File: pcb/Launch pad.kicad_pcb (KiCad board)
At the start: 2 copper layers, 86 x 90.3 mm, 13 parts, among them SW10 SW_Push, SW11 SW_Push, SW12 SW_Push, SW13 SW_Push, SW7 SW_Push, SW9 SW_Push, U1 XIAO-RP2040-DIP

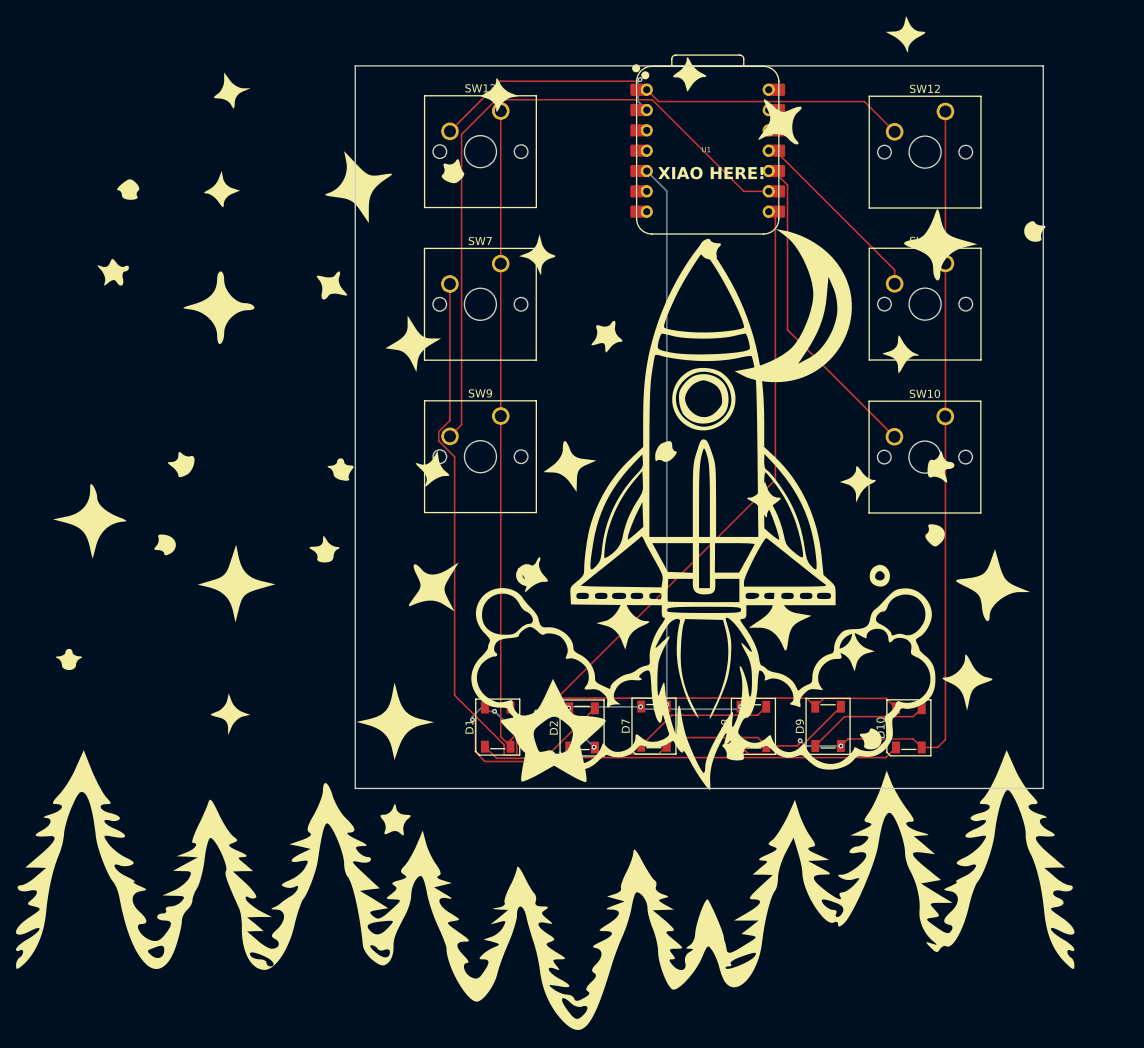
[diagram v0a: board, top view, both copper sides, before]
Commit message: added firmware
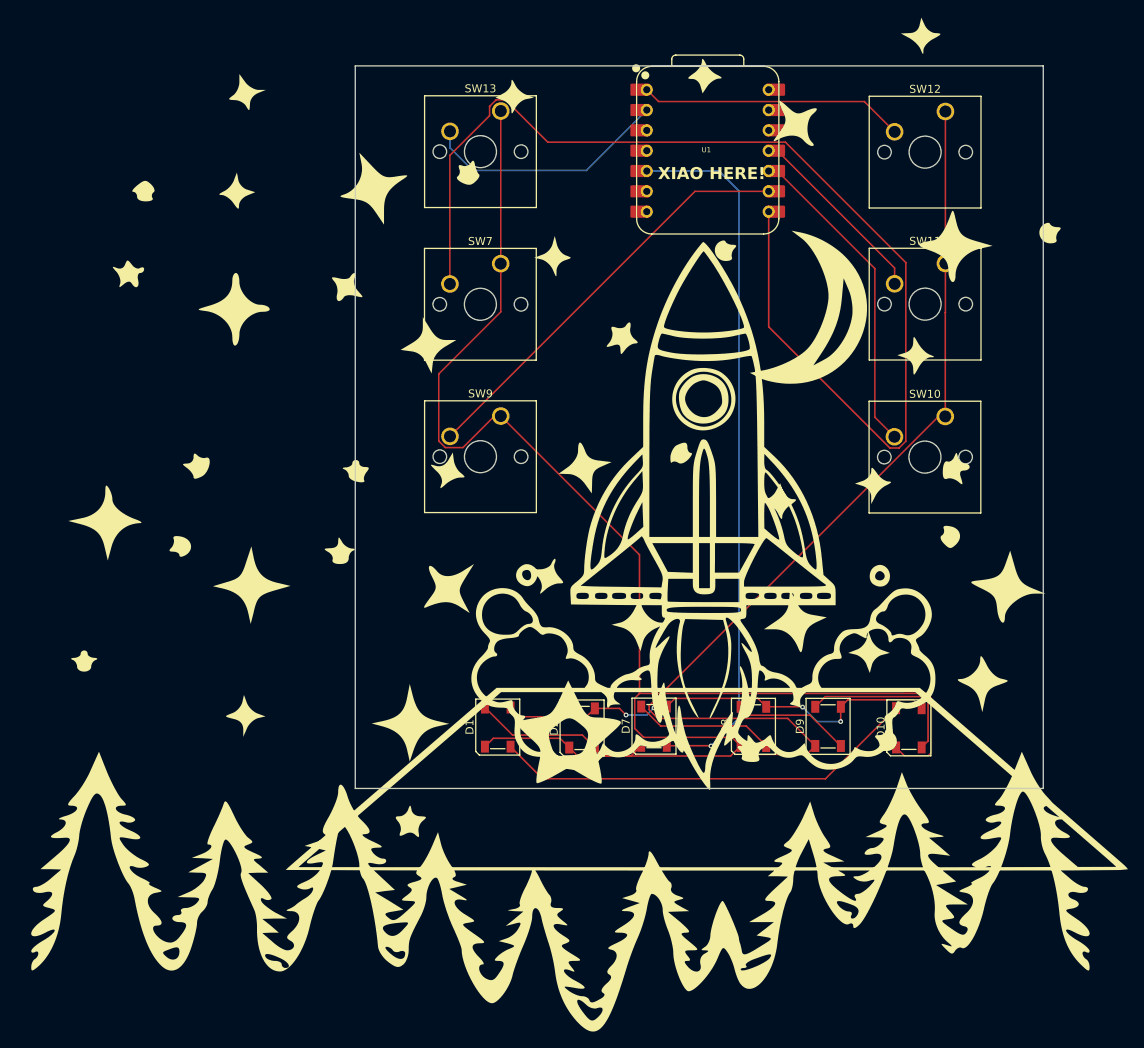
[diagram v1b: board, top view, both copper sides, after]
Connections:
- D1 pad 1: Net-(D1-VSS) -> GND
- D1 pad 2: GND -> Net-(D1-DIN)
- D1 pad 3: Net-(D1-VDD) -> +5V
- D1 pad 4: +5V -> Net-(D1-DOUT)
- D10 pad 1: Net-(D1-VDD) -> GND
- D10 pad 2: GND -> Net-(D10-DIN)
- D10 pad 3: Net-(D10-VDD) -> +5V
- D10 pad 4: +5V -> Net-(D1-DIN)
- D2 pad 1: unconnected-(D2-VSS-Pad1) -> GND
- D2 pad 2: GND -> Net-(D1-DOUT)
- D2 pad 3: Net-(D1-VSS) -> +5V
- D2 pad 4: +5V -> unconnected-(D2-DOUT-Pad4)
- D7 pad 1: Net-(D7-VSS) -> GND
- D7 pad 2: GND -> Net-(D7-DIN)
- D7 pad 3: Net-(D7-VDD) -> +5V
- D7 pad 4: +5V -> Net-(D7-DOUT)
- D8 pad 1: Net-(D8-VSS) -> GND
- D8 pad 2: GND -> Net-(D7-DOUT)
- D8 pad 3: Net-(D7-VSS) -> +5V
- D8 pad 4: +5V -> Net-(D8-DOUT)
- D9 pad 1: Net-(D10-VDD) -> GND
- D9 pad 2: GND -> Net-(D8-DOUT)
- D9 pad 3: Net-(D8-VSS) -> +5V
- D9 pad 4: +5V -> Net-(D10-DIN)
- U1 pad 5: Net-(D7-VDD) -> Net-(D7-DIN)
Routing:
- net GND: track 220.8 -> 329.1 mm, vias 4 -> 0
- net Net-(D7-DIN): track 0.00 -> 88.9 mm, vias 0 -> 1
- net Net-(D7-VDD): track 68.2 -> 0.00 mm, vias 1 -> 0
- net Net-(D1-VDD): track 64.1 -> 0.00 mm, vias 2 -> 0
- net Net-(D1-DIN): track 0.00 -> 53.5 mm
- net Net-(U1-GPIO2/SCK): track 84.1 -> 52.5 mm
- net +5V: track 81.0 -> 57.3 mm, vias 5 -> 4
- net Net-(D10-DIN): track 0.00 -> 21.1 mm
- net Net-(D7-DOUT): track 0.00 -> 17.7 mm
- net Net-(D7-VSS): track 17.6 -> 0.00 mm
- net Net-(D1-VSS): track 16.9 -> 0.00 mm
- net Net-(D1-DOUT): track 0.00 -> 15.8 mm
- net Net-(D8-VSS): track 15.4 -> 0.00 mm
- net Net-(D10-VDD): track 15.3 -> 0.00 mm
- net Net-(D8-DOUT): track 0.00 -> 14.6 mm
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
